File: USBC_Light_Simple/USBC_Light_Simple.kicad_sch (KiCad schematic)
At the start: 0 parts

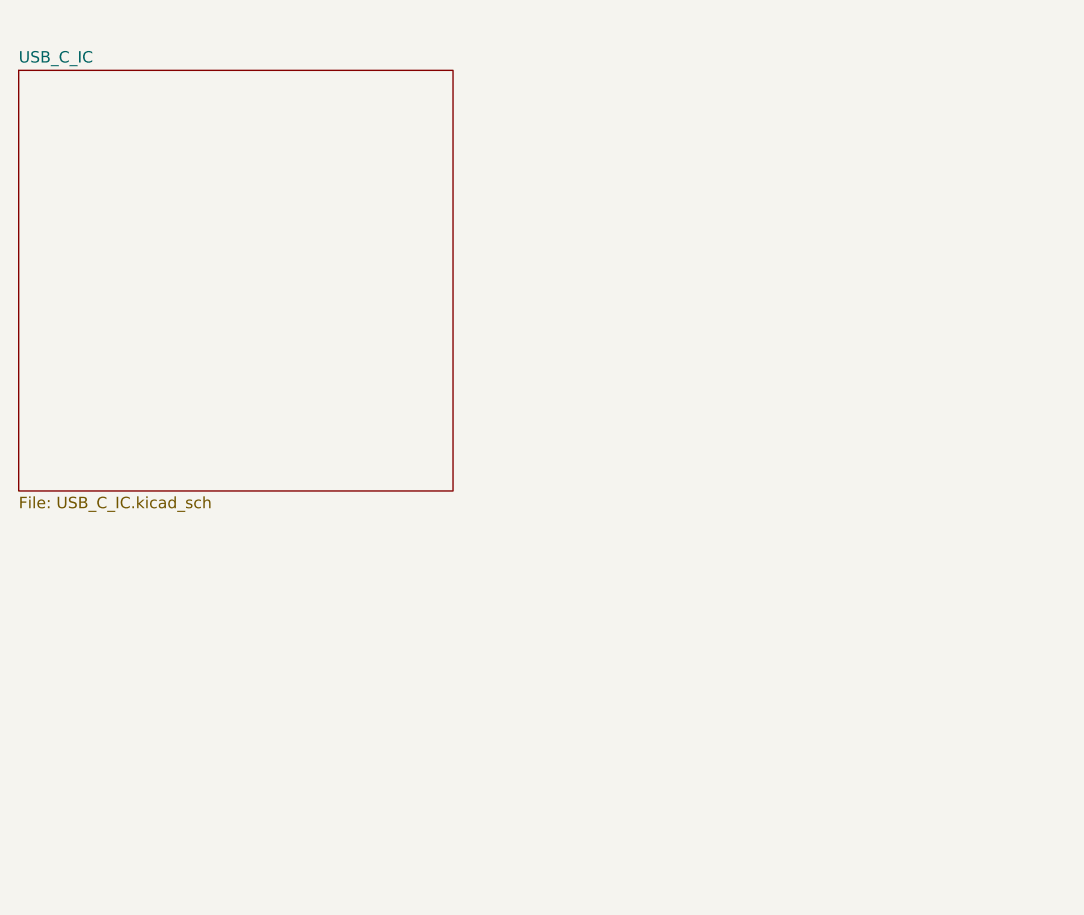
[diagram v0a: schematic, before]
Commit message: Continued work:
- Added LED driver and STM32
- Began basic layout
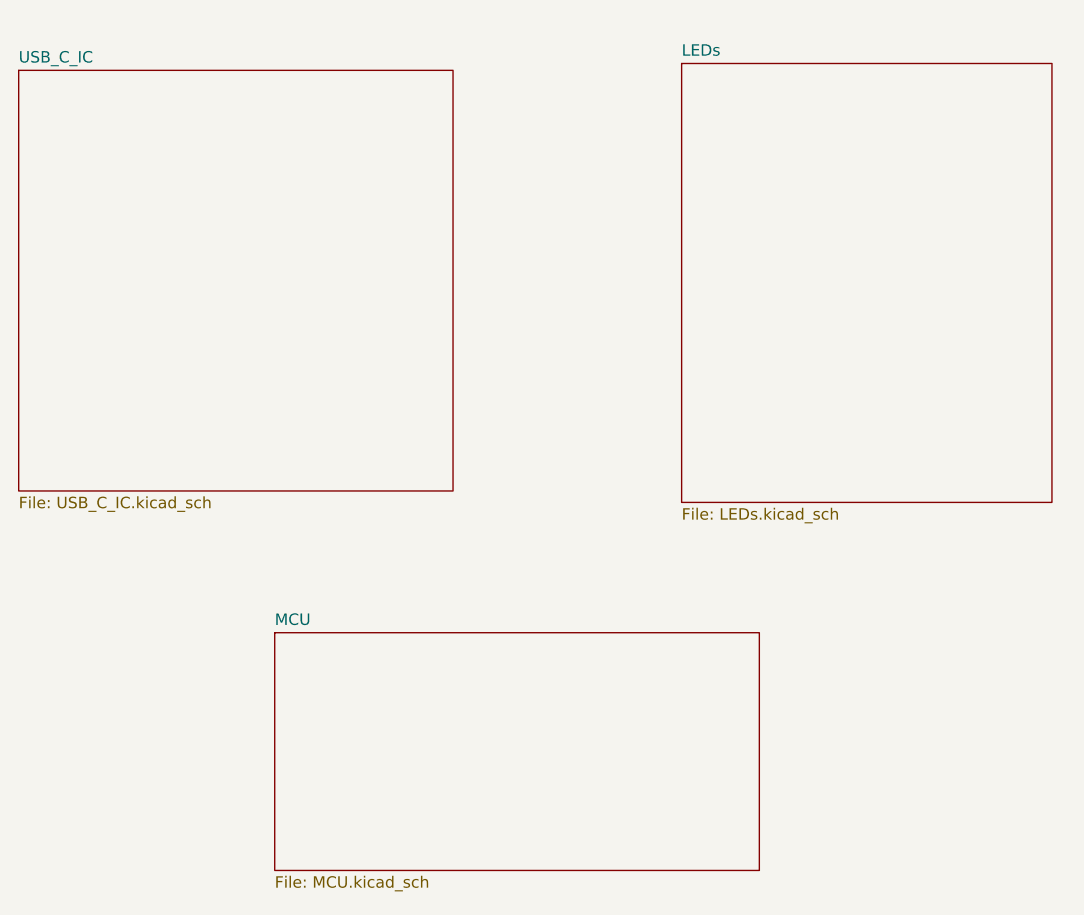
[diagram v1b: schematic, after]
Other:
- added sheet LEDs (LEDs.kicad_sch)
- added sheet MCU (MCU.kicad_sch)
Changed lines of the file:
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@@
+		)
+	)
+	(sheet
+		(at 101.854 105.156)
+		(size 53.848 26.416)
+		(exclude_from_sim no)
+		(in_bom yes)
+		(on_board yes)
+		(dnp no)
+		(fields_autoplaced yes)
+		(stroke
+			(width 0.1524)
+			(type solid)
+		)
+		(fill
+			(color 0 0 0 0.0000)
+		)
+		(property "Sheetname" "MCU"
+			(at 101.854 104.4444 0)
+			(effects
+				(font
+					(size 1.27 1.27)
+				)
+				(justify left bottom)
+			)
+		)
+		(property "Sheetfile" "MCU.kicad_sch"
+			(at 101.854 132.1566 0)
+			(effects
+				(font
+					(size 1.27 1.27)
+				)
+				(justify left top)
+			)
+		)
+		(instances
+			(project "USBC_Light_Simple"
+				(path "/df06901f-4c94-45fd-9b10-d1e99011d9f7"
+					(page "4")
+				)
+			)
+		)
+	)
+	(sheet
+		(at 147.066 41.91)
+		(size 41.148 48.768)
+		(exclude_from_sim no)
+		(in_bom yes)
+		(on_board yes)
+		(dnp no)
+		(fields_autoplaced yes)
+		(stroke
+			(width 0.1524)
+			(type solid)
+		)
+		(fill
+			(color 0 0 0 0.0000)
+		)
+		(property "Sheetname" "LEDs"
+			(at 147.066 41.1984 0)
+			(effects
+				(font
+					(size 1.27 1.27)
+				)
+				(justify left bottom)
+			)
+		)
+		(property "Sheetfile" "LEDs.kicad_sch"
+			(at 147.066 91.2626 0)
+			(effects
+				(font
+					(size 1.27 1.27)
+				)
+				(justify left top)
+			)
+		)
+		(instances
+			(project "USBC_Light_Simple"
+				(path "/df06901f-4c94-45fd-9b10-d1e99011d9f7"
+					(page "3")
+				)
+			)
 		)
 	)

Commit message: Fleshed out most of schematic. Now need to add component vals.
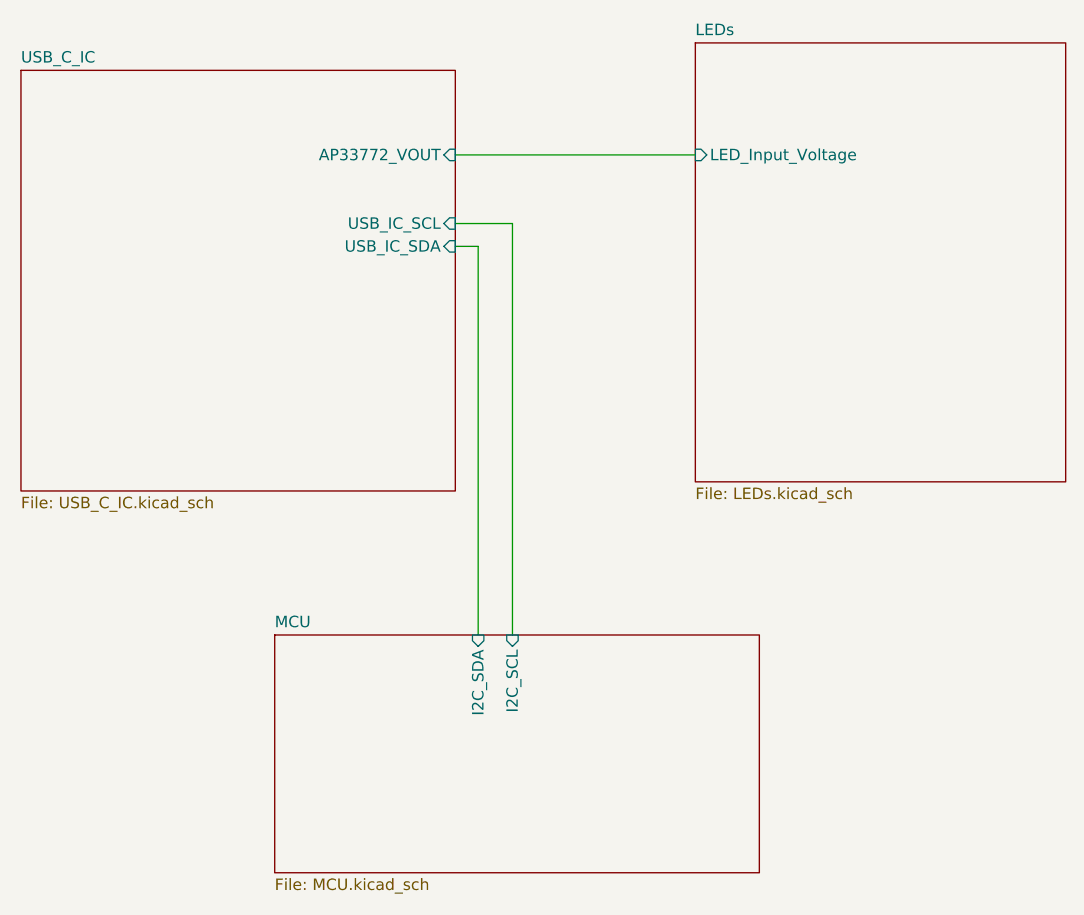
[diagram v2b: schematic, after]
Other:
- sheet LEDs ports: added LED_Input_Voltage; removed none
- sheet MCU ports: added I2C_SCL, I2C_SDA; removed none
- sheet USB_C_IC ports: added AP33772_VOUT, USB_IC_SCL, USB_IC_SDA; removed none
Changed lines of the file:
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@@
 	(generator_version "9.0")
 	(paper "A4")
+	(wire
+		(pts
+			(xy 128.27 59.69) (xy 121.92 59.69)
+		)
+		(stroke
+			(width 0)
+			(type default)
+		)
+	)
+	(wire
+		(pts
+			(xy 121.92 62.23) (xy 124.46 62.23)
+		)
+		(stroke
+			(width 0)
+			(type default)
+		)
+	)
+	(wire
+		(pts
+			(xy 121.92 52.07) (xy 148.59 52.07)
+		)
+		(stroke
+			(width 0)
+			(type default)
+		)
+	)
+	(wire
+		(pts
+			(xy 124.46 62.23) (xy 124.46 105.41)
+		)
+		(stroke
+			(width 0)
+			(type default)
+		)
+	)
+	(wire
+		(pts
+			(xy 128.27 105.41) (xy 128.27 59.69)
+		)
+		(stroke
+			(width 0)
+			(type default)
+		)
+	)
 	(sheet
-		(at 73.406 42.672)
+		(at 73.66 42.672)
 		(size 48.26 46.736)
 		(exclude_from_sim no)
@@
 		)
 		(property "Sheetname" "USB_C_IC"
-			(at 73.406 41.9604 0)
+			(at 73.66 41.9604 0)
 			(effects
 				(font
@@
 		)
 		(property "Sheetfile" "USB_C_IC.kicad_sch"
-			(at 73.406 89.9926 0)
+			(at 73.66 89.9926 0)
 			(effects
 				(font
@@
 				)
 				(justify left top)
+			)
+		)
+		(pin "AP33772_VOUT" input
+			(at 121.92 52.07 0)
+			(effects
+				(font
+					(size 1.27 1.27)
+				)
+				(justify right)
+			)
+		)
+		(pin "USB_IC_SCL" input
+			(at 121.92 59.69 0)
+			(effects
+				(font
+					(size 1.27 1.27)
+				)
+				(justify right)
+			)
+		)
+		(pin "USB_IC_SDA" input
+			(at 121.92 62.23 0)
+			(effects
+				(font
+					(size 1.27 1.27)
+				)
+				(justify right)
 			)
 		)
@@
 	)
 	(sheet
-		(at 101.854 105.156)
+		(at 101.854 105.41)
 		(size 53.848 26.416)
 		(exclude_from_sim no)
@@
 		)
 		(property "Sheetname" "MCU"
-			(at 101.854 104.4444 0)
+			(at 101.854 104.6984 0)
 			(effects
 				(font
@@
 		)
 		(property "Sheetfile" "MCU.kicad_sch"
-			(at 101.854 132.1566 0)
+			(at 101.854 132.4106 0)
 			(effects
 				(font
@@
 				)
 				(justify left top)
+			)
+		)
+		(pin "I2C_SCL" input
+			(at 128.27 105.41 90)
+			(effects
+				(font
+					(size 1.27 1.27)
+				)
+				(justify right)
+			)
+		)
+		(pin "I2C_SDA" input
+			(at 124.46 105.41 90)
+			(effects
+				(font
+					(size 1.27 1.27)
+				)
+				(justify right)
 			)
 		)
@@
 	)
 	(sheet
-		(at 147.066 41.91)
+		(at 148.59 39.624)
 		(size 41.148 48.768)
 		(exclude_from_sim no)
@@
 		)
 		(property "Sheetname" "LEDs"
-			(at 147.066 41.1984 0)
+			(at 148.59 38.9124 0)
 			(effects
 				(font
@@
 		)
 		(property "Sheetfile" "LEDs.kicad_sch"
-			(at 147.066 91.2626 0)
+			(at 148.59 88.9766 0)
 			(effects
 				(font
@@
 			)
 		)
+		(pin "LED_Input_Voltage" input
+			(at 148.59 52.07 180)
+			(effects
+				(font
+					(size 1.27 1.27)
+				)
+				(justify left)
+			)
+		)
